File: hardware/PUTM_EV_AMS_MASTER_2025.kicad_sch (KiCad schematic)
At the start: 45 parts, among them IC11 ISO6760, IC7 ISO6760, IC8 3.3V/0.5A, J1 M80-5100642, J10 M300-MV10345M1, J12 M80-51034XX, J2 USB_C_Receptacle_USB2.0_14P, J3 M80-51014XX, J4 FTSH-107-01-L-D-K, J5 M80-51004XX, J7 M300-MV10345M1, J8 M80-51004XX, U4 UCC12040DVE

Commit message: inductors 3d models fix, smaller relay (same series as the one from IMD), other + sync
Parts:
- removed D17, D18, D19, D20: 1.7V/1kV, Diode_SMD:D_SMA, symbol Device:D_Small
- removed F1: 5V/0.5A, Fuse:Fuse_0805_2012Metric, symbol Device:Fuse_Small
- removed F10, F11, F12, F13, F14, F15, F9: ?A/600V, symbol Device:Fuse_Small
- added C43, C50: 10nF/1kV, Capacitor_SMD:C_1206_3216Metric, symbol c2824c562jggacauto:C2824C562JGGACAUTO
- F6, F7: symbol Device:Fuse_Small -> Device:Polyfuse_Small
- TP1: footprint Connector_Pin:Pin_D0.7mm_L6.5mm_W1.8mm_FlatFork -> TestPoint:TestPoint_Pad_D1.0mm
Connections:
- net +5VISO is gone; now on net I_VDDISO: F7.1
- net +3.3VISO: now also F6.2; no longer F6.1
- net F_+3VISO: now also F6.1; no longer F6.2
- net GNDISO: now also C50.2; no longer C36.1
- net Isolated ADC/ACU_V+: now also J7.1 (Pin_1)
- net Isolated ADC/ACU_V-: now also J7.3 (Pin_3)
- net Isolated ADC/CAR_V+: now also J10.1 (Pin_1)
- net Isolated ADC/CAR_V-: now also J10.3 (Pin_3)
- net Isolated SPI/OUT+: now also C43.2
- net Isolated SPI/OUT-: now also C36.2
- net at J5.1 (Pin_1): now also C36.1
- net at J5.2 (Pin_2): now also C43.1
- net SHIELD renamed ISO_SPI_SH
- net ISO_SPI_SH: now also C50.1
- no-connect marks 22 -> 24
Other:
- sheet Connectivity ports: added none; removed AIR1_I, AIR1_O, AIR2_I, AIR2_O, AIR3_I, AIR3_O, CANFD1+, CANFD1-, CANFD1_RX, CANFD1_TX, CANFD2+, CANFD2-, CANFD2_RX, CANFD2_TX, CANFD3+, CANFD3-, CANFD3_RX, CANFD3_TX, D+_I, D+_O, D-_I, D-_O, MV_I1, MV_I2, MV_I3, MV_O1, MV_O2, MV_O3, SPI_I1, SPI_I2, SPI_I3, SPI_I4, SPI_O1, SPI_O2, SPI_O3, SPI_O4
- sheet MCU ports: added EN_12V, PG_12V; removed none
- sheet Power ports: added EN_12V, PG_12V; removed none
- note added: "CONNECTORS"
- note removed: "HV CONNECTORS"
- note removed: "ISO CONNECTORS"
- moved on the sheet: D1, D2, D3, D6, J10, J5, J7, J8, RN16A, RN16B, RN16C, RN16D

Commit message: all but the communications sections done
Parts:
- removed C50: 10nF/1kV, Capacitor_SMD:C_1206_3216Metric, symbol c2824c562jggacauto:C2824C562JGGACAUTO
- removed C53: 5.6nF/2000V, Capacitor_SMD:C_3640_9110Metric, symbol c2824c562jggacauto:C2824C562JGGACAUTO
- removed RN16: 1k, Resistor_SMD:R_Array_Convex_4x0603, symbol Device:R_Pack04_Split
- added R27, R31, R34, R36: 1k, Resistor_SMD:R_0603_1608Metric, symbol Device:R_Small
- D15: footprint (none) -> Diode_SMD:D_SOD-123
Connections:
- net AMS_ERR: now also R36.2
- net AMS_ERROR: now also R36.1
- net LED1: now also R27.2
- net LED2: now also R31.2
- net LED3: now also R34.2
- net SIGNAL_LED_1: now also R27.1
- net SIGNAL_LED_2: now also R31.1
- net SIGNAL_LED_3: now also R34.1
- net IMD_SENSENSOR renamed IMD_SENSOR
- net ISO_SPI_SH: no longer names the net of J5.3 (Pin_3), J5.4 (Pin_4)
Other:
- moved on the sheet: C36, C43, J5

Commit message: sync
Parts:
- removed C36, C43: 10nF/1kV, Capacitor_SMD:C_1206_3216Metric, symbol c2824c562jggacauto:C2824C562JGGACAUTO
- added R91, R92: 5.1k, Resistor_SMD:R_0603_1608Metric, symbol Device:R_Small
- added T1: >100kHz, Samacsys:SOP254P914X350-4N, symbol Samacsys_kicad_sym:ESMIT-4180_C
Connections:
- net GND: now also R91.1, R92.1
- net Isolated SPI/OUT+: now also T1.4
- net Isolated SPI/OUT-: now also T1.3
- net at J5.1 (Pin_1): now also T1.2
- net at J5.2 (Pin_2): now also T1.1
- net at J5.3 (Pin_3): no longer J5.4 (Pin_4)
- net at J2.A5 (CC1): now also R91.2
- net at J2.B5 (CC2): now also R92.2
- net IMD_SENSOR: no longer names the net of J12.30 (Pin_30)
- net ISO_LTC_MISO renamed ISO_COM_MISO
- net ISO_LTC_MOSI renamed ISO_COM_MOSI
- net ISO_LTC_SCK renamed ISO_COM_SCK
- net I_VDDISO renamed +5VISO
- net MCU/LTC_MISO renamed MCU/COM_MISO
- net MCU/LTC_MOSI renamed MCU/COM_MOSI
- net MCU/LTC_SCK renamed MCU/COM_SCK
- net MCU/~{LTC_CS} renamed MCU/~{COM_CS}
- net ~{ISO_LTC_CS} renamed ~{ISO_COM_CS}
- no-connect marks 24 -> 25
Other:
- sheet Connectivity ports: added EX_AIR_AUX_M, EX_AIR_AUX_P, EX_AIR_AUX_PRE, EX_CANFD1+, EX_CANFD1-, EX_CANFD2+, EX_CANFD2-, EX_CANFD3+, EX_CANFD3-, EX_D+, EX_D-, EX_IN1, EX_IN2, EX_SPI_CS, EX_SPI_MISO, EX_SPI_MOSI, EX_SPI_SCK, UC_AIR_AUX_M, UC_AIR_AUX_P, UC_AIR_AUX_PRE, UC_CANFD1_RX, UC_CANFD1_TX, UC_CANFD2_RX, UC_CANFD2_TX, UC_CANFD3_RX, UC_CANFD3_TX, UC_D+, UC_D-, UC_IN1, UC_IN2, UC_SPI_CS, UC_SPI_MISO, UC_SPI_MOSI, UC_SPI_SCK; removed none
- sheet MCU ports: added COM_MISO, COM_MOSI, COM_SCK, ~{COM_CS}; removed LTC_MISO, LTC_MOSI, LTC_SCK, SENS_IMD, ~{LTC_CS}
- moved on the sheet: D15, J1, J2, J5

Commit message: sync
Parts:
- C39, C44, C45, C46, C47, C48: Mouser Price/Stock (none) -> https://www.mouser.pl/ProductDetail/KEMET/C0603C104J3RACTU?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
- C40, C59: Mouser Price/Stock (none) -> https://www.mouser.pl/ProductDetail/Samsung-Electro-Mechani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
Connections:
- net GNDISO: no longer IC11.5 (IND), IC11.6 (INE)
- net CCO+: now reaches J5.1 (Pin_1), T1.2
- net CCO-: now reaches J5.2 (Pin_2), T1.1
- net MCU/~{FLT}: now reaches IC11.11 (OUTE)
- net MCU/SPI_RDY: now reaches IC11.12 (OUTD)
- net Isolated SPI/OUT+ renamed OUT-
- net Isolated SPI/OUT- renamed OUT+
- new net SPI_RDY: IC11.5 (IND)
- new net ~{FLT}: IC11.6 (INE)
- no-connect marks 25 -> 23
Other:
- sheet Isolated SPI ports: added SPI_RDY, ~{FLT}; removed none
- sheet MCU ports: added SPI_RDY, ~{FLT}; removed none
- note added: "SHARED"
- note added: "TI_IC ONLY"
- moved on the sheet: J5, T1

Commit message: the connectors wil stay and wont be changed further
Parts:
- added TP4, TP5, TP6, TP7, TP8: TestPoint_Small, TestPoint:TestPoint_THTPad_D1.0mm_Drill0.5mm, symbol Connector:TestPoint_Small
- TP1: footprint TestPoint:TestPoint_Pad_D1.0mm -> TestPoint:TestPoint_THTPad_D1.0mm_Drill0.5mm
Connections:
- net AIR_M_DETECTION: now also J12.23 (Pin_23); no longer J12.13 (Pin_13)
- net AIR_PRE_DETECTION: now also J12.22 (Pin_22); no longer J12.12 (Pin_12)
- net AIR_P_DETECTION: now also J12.24 (Pin_24); no longer J12.14 (Pin_14)
- net CANFD1+: now also J12.7 (Pin_7); no longer J12.27 (Pin_27)
- net CANFD1-: now also J12.8 (Pin_8); no longer J12.26 (Pin_26)
- net CANFD2+: now also J12.5 (Pin_5); no longer J12.25 (Pin_25)
- net CANFD2-: now also J12.6 (Pin_6); no longer J12.24 (Pin_24)
- net CANFD3+: now also J12.3 (Pin_3); no longer J12.23 (Pin_23)
- net CANFD3-: now also J12.4 (Pin_4); no longer J12.22 (Pin_22)
- net CCO+: now also TP7.1
- net CCO-: now also TP8.1
- net CHARGER_DETECTION: now also J12.20 (Pin_20); no longer J12.10 (Pin_10)
- net D+: now also J12.32 (Pin_32); no longer J12.17 (Pin_17)
- net D-: now also J12.31 (Pin_31); no longer J12.16 (Pin_16)
- net EXT_MISO: now also J12.14 (Pin_14); no longer J12.33 (Pin_33)
- net EXT_MOSI: now also J12.13 (Pin_13); no longer J12.32 (Pin_32)
- net EXT_SCK: now also J12.12 (Pin_12); no longer J12.31 (Pin_31)
- net F_+3VISO: now also TP6.1
- net F_+5VISO: now also TP4.1
- net GND: now also J12.16 (Pin_16), J12.33 (Pin_33); no longer J12.20 (Pin_20), J12.3 (Pin_3)
- net GNDISO: now also TP5.1
- net SAFETY1: now also J12.10 (Pin_10); no longer J12.5 (Pin_5)
- net SAFETY2: now also J12.11 (Pin_11); no longer J12.6 (Pin_6)
- net VDD: now also J12.17 (Pin_17), J12.34 (Pin_34); no longer J12.19 (Pin_19), J12.2 (Pin_2)
- net ~{EXT_CS}: now also J12.15 (Pin_15); no longer J12.34 (Pin_34)
- no-connect marks 23 -> 16
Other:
- moved on the sheet: C40, C47, C48, F6, F7, IC8, J12, R22, TP1

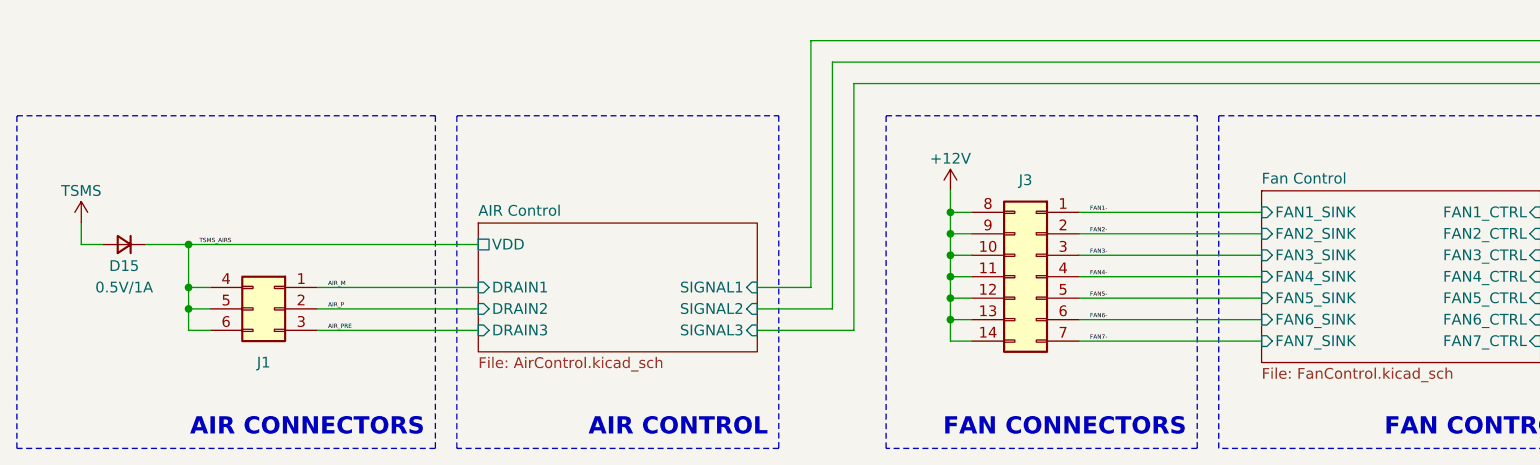
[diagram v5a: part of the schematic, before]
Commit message: LV section component placement done
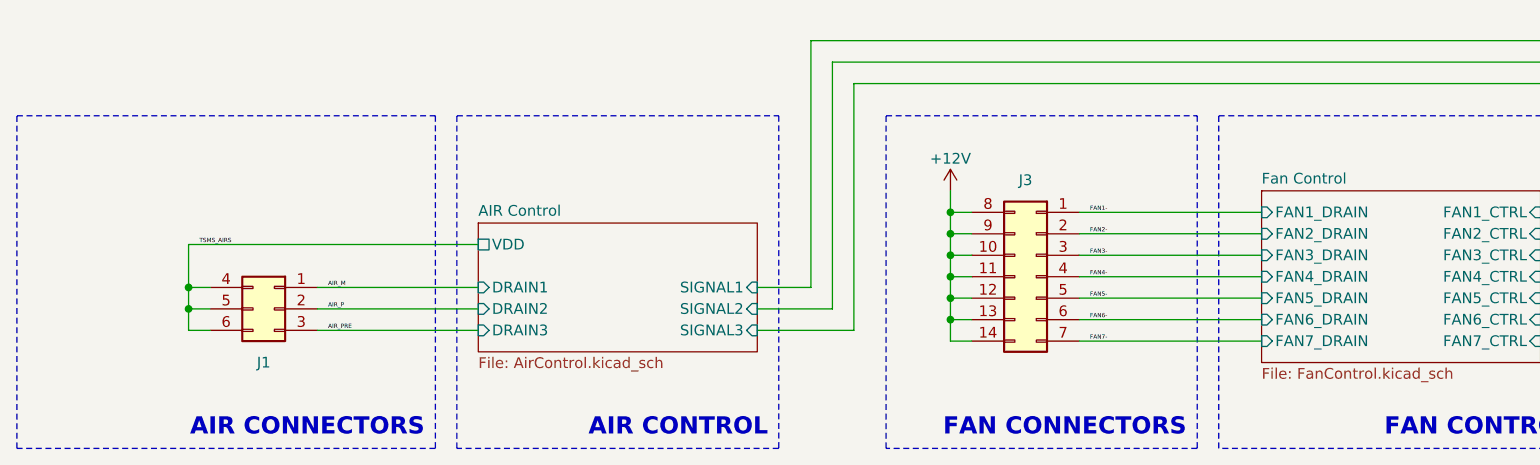
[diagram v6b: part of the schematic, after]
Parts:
- removed D15: 0.5V/1A, Diode_SMD:D_SOD-123, symbol Device:D_Small
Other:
- sheet Fan Control ports: added FAN1_DRAIN, FAN2_DRAIN, FAN3_DRAIN, FAN4_DRAIN, FAN5_DRAIN, FAN6_DRAIN, FAN7_DRAIN; removed FAN1_SINK, FAN2_SINK, FAN3_SINK, FAN4_SINK, FAN5_SINK, FAN6_SINK, FAN7_SINK
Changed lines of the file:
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@@
 	)
 	(junction
-		(at 35.56 257.81)
-		(diameter 0)
-		(color 0 0 0 0)
-	)
-	(junction
 		(at 367.03 133.35)
 		(diameter 0)
@@
 	(wire
 		(pts
-			(xy 22.86 257.81) (xy 25.4 257.81)
-		)
-		(stroke
-			(width 0)
-			(type default)
-		)
-	)
-	(wire
-		(pts
 			(xy 38.1 262.89) (xy 35.56 262.89)
 		)
@@
 	(wire
 		(pts
-			(xy 22.86 255.27) (xy 22.86 257.81)
-		)
-		(stroke
-			(width 0)
-			(type default)
-		)
-	)
-	(wire
-		(pts
 			(xy 173.99 146.05) (xy 213.36 146.05)
 		)
@@
 	(wire
 		(pts
-			(xy 30.48 257.81) (xy 35.56 257.81)
-		)
-		(stroke
-			(width 0)
-			(type default)
-		)
-	)
-	(wire
-		(pts
 			(xy 304.8 193.04) (xy 307.34 193.04)
 		)
@@
 	)
 	(symbol
-		(lib_id "Device:D_Small")
-		(at 27.94 257.81 0)
-		(mirror y)
-		(unit 1)
-		(exclude_from_sim no)
-		(in_bom yes)
-		(on_board yes)
-		(dnp no)
-		(property "Reference" "D15"
-			(at 27.94 260.35 0)
-			(effects
-				(font
-					(size 1.27 1.27)
-				)
-			)
-		)
-		(property "Value" "0.5V/1A"
-			(at 27.94 262.89 0)
-			(effects
-				(font
-					(size 1.27 1.27)
-				)
-			)
-		)
-		(property "Footprint" "Diode_SMD:D_SOD-123"
-			(at 27.94 257.81 90)
-			(effects
-				(font
-					(size 1.27 1.27)
-				)
-				(hide yes)
-			)
-		)
-		(property "Datasheet" "~"
-			(at 27.94 257.81 90)
-			(effects
-				(font
-					(size 1.27 1.27)
-				)
-				(hide yes)
-			)
-		)
-		(property "Description" "Diode, small symbol"
-			(at 27.94 257.81 0)
-			(effects
-				(font
-					(size 1.27 1.27)
-				)
-				(hide yes)
-			)
-		)
-		(pin "1"
-		)
-		(pin "2"
-		)
-		(instances
-			(project "PUTM_EV_BMS_HV_MASTER_2023"
-				(path "/b456cffc-d9d7-4c91-91f2-36ec9a65dd1b"
-					(reference "D15")
-					(unit 1)
-				)
-			)
-		)
-	)
-	(symbol
 		(lib_name "GND_22")
 		(lib_id "power:GND")
@@
 	)
 	(symbol
-		(lib_name "+5V_1")
-		(lib_id "power:+5V")
-		(at 22.86 255.27 0)
-		(mirror y)
-		(unit 1)
-		(exclude_from_sim no)
-		(in_bom yes)
-		(on_board yes)
-		(dnp no)
-		(property "Reference" "#PWR082"
-			(at 22.86 259.08 0)
-			(effects
-				(font
-					(size 1.27 1.27)
-				)
-				(hide yes)
-			)
-		)
-		(property "Value" "TSMS"
-			(at 22.86 251.46 0)
-			(effects
-				(font
-					(size 1.27 1.27)
-				)
-			)
-		)
-		(property "Footprint" ""
-			(at 22.86 255.27 0)
-			(effects
-				(font
-					(size 1.27 1.27)
-				)
-				(hide yes)
-			)
-		)
-		(property "Datasheet" ""
-			(at 22.86 255.27 0)
-			(effects
-				(font
-					(size 1.27 1.27)
-				)
-				(hide yes)
-			)
-		)
-		(property "Description" ""
-			(at 22.86 255.27 0)
-			(effects
-				(font
-					(size 1.27 1.27)
-				)
-				(hide yes)
-			)
-		)
-		(pin "1"
-		)
-		(instances
-			(project "PUTM_EV_BMS_HV_MASTER_2023"
-				(path "/b456cffc-d9d7-4c91-91f2-36ec9a65dd1b"
-					(reference "#PWR082")
-					(unit 1)
-				)
-			)
-		)
-	)
-	(symbol
 		(lib_name "GND_28")
 		(lib_id "power:GND")
@@
 			)
 		)
-		(pin "FAN4_SINK" input
+		(pin "FAN4_DRAIN" input
 			(at 162.56 261.62 180)
 			(effects
@@
 			)
 		)
-		(pin "FAN6_SINK" input
+		(pin "FAN6_DRAIN" input
 			(at 162.56 266.7 180)
 			(effects
@@
 			)
 		)
-		(pin "FAN5_SINK" input
+		(pin "FAN5_DRAIN" input
 			(at 162.56 264.16 180)
 			(effects
@@
 			)
 		)
-		(pin "FAN7_SINK" input
+		(pin "FAN7_DRAIN" input
 			(at 162.56 269.24 180)
 			(effects
@@
 			)
 		)
-		(pin "FAN1_SINK" input
+		(pin "FAN1_DRAIN" input
 			(at 162.56 254 180)
 			(effects
@@
 			)
 		)
-		(pin "FAN2_SINK" input
+		(pin "FAN2_DRAIN" input
 			(at 162.56 256.54 180)
 			(effects
@@
 			)
 		)
-		(pin "FAN3_SINK" input
+		(pin "FAN3_DRAIN" input
 			(at 162.56 259.08 180)
 			(effects

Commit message: sync
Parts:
- added C77: 22uF, Capacitor_SMD:C_0805_2012Metric, symbol Device:C_Small
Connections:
- net F_+5VISO: now also C77.1
- net GNDISO: now also C77.2
- net SAFETY1 renamed SAFETY_IN
- net SAFETY2 renamed SAFETY_OUT
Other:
- sheet Safety ports: added SAFETY_IN, SAFETY_OUT; removed SAFETY1, SAFETY2
- moved on the sheet: C40

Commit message: some routing done
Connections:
- no-connect marks 16 -> 23
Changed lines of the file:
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@@
+	)
+	(no_connect
+		(at 374.65 213.36)
+	)
+	(no_connect
+		(at 374.65 218.44)
 	)
 	(no_connect
@@
 	)
 	(no_connect
+		(at 374.65 215.9)
+	)
+	(no_connect
+		(at 374.65 203.2)
+	)
+	(no_connect
 		(at 361.95 215.9)
 	)
 	(no_connect
+		(at 374.65 220.98)
+	)
+	(no_connect
 		(at 375.92 76.2)
+	)
+	(no_connect
+		(at 374.65 223.52)
 	)
 	(no_connect
@@
 	)
 	(no_connect
+		(at 374.65 226.06)
+	)
+	(no_connect
